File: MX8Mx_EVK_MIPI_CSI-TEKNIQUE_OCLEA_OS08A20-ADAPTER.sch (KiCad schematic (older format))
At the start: 16 parts, among them J1 1888863-4, J2 3-1734592-2, U1 NLSX5014DTR2G, U2 SN74LVC1G14DRL

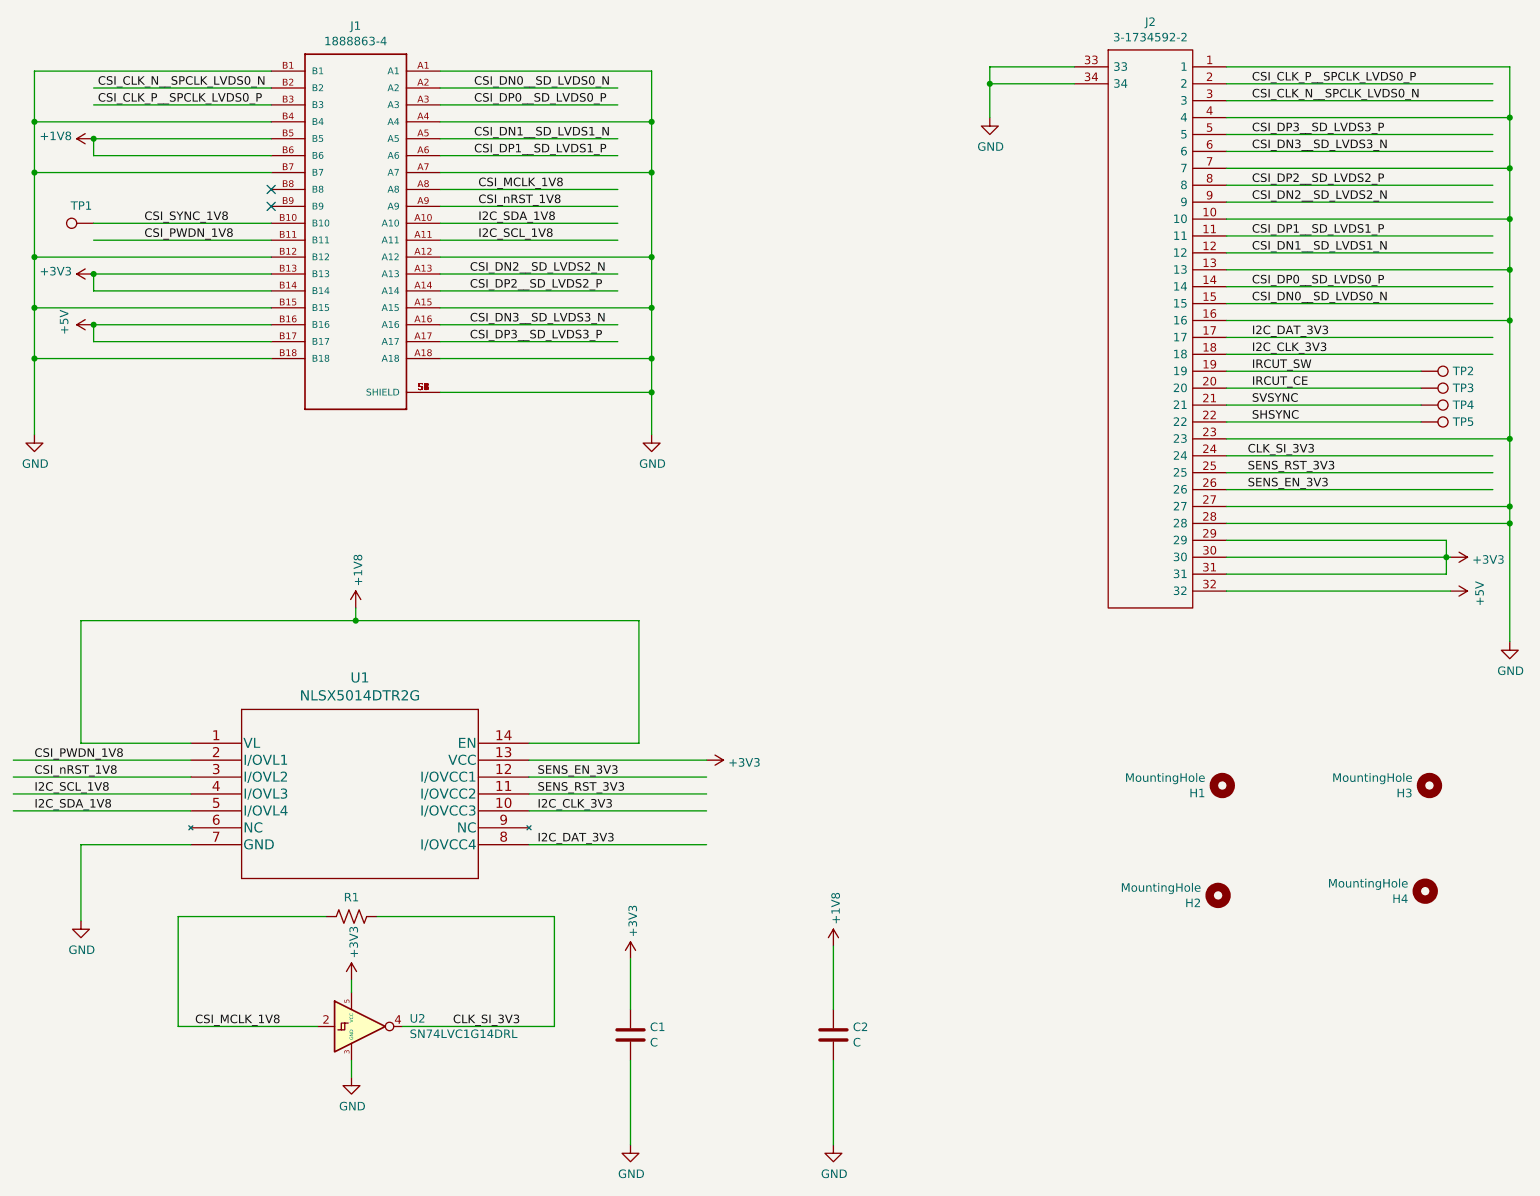
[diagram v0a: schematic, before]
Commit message: Update design with separate I2C and GPIO level translators
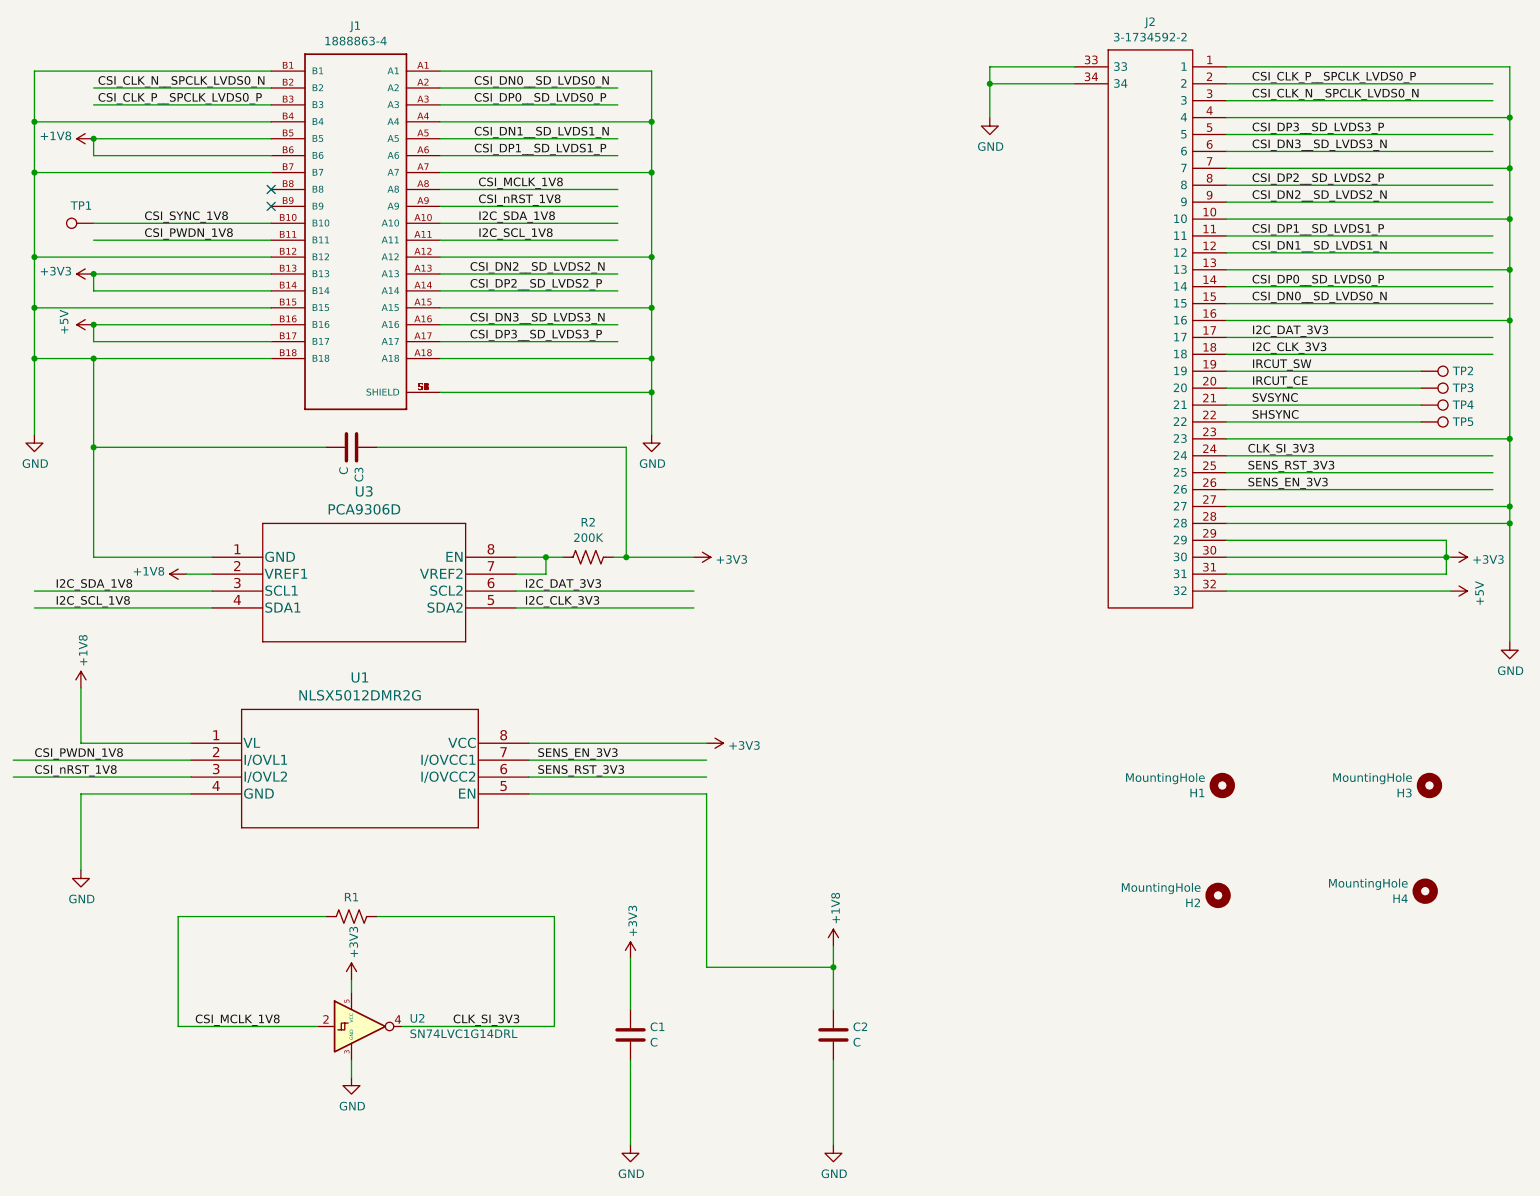
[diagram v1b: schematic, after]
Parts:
- removed U1: NLSX5014DTR2G, footprints:NLSX5014DTR2G, symbol NLSX5014DTR2G:NLSX5014DTR2G
- added C3: C, Capacitor_SMD:C_0603_1608Metric_Pad1.08x0.95mm_HandSolder, symbol Device:C
- added R2: 200K, Resistor_SMD:R_0805_2012Metric_Pad1.20x1.40mm_HandSolder, symbol Device:R_US
- added U1: NLSX5012DMR2G, footprints:NLSX5012DMR2G, symbol NLSX5012DMR2G:NLSX5012DMR2G
- added U3: PCA9306D, footprints:PCA9306D, symbol PCA9306D:PCA9306D_118
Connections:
- wire segments 129 -> 142
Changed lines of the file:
@@
 Sheet 1 1
 Title "Adapter for TEKNIQUE Oclea OS08a20 to MX8M Mini/Plus EVK"
-Date "2021-11-10"
-Rev "V1A"
+Date "2021-11-11"
+Rev "V1B"
 Comp "TuxVision"
 Comment1 ""
@@
 I2C_SCL_1V8
 $Comp
-L NLSX5014DTR2G:NLSX5014DTR2G U1
-U 1 1 6158CD6A
-P 1775 5050
-F 0 "U1" H 2775 5437 60  0000 C CNN
-F 1 "NLSX5014DTR2G" H 2775 5331 60  0000 C CNN
-F 2 "footprints:NLSX5014DTR2G" H 2775 5290 60  0001 C CNN
-F 3 "" H 1775 5050 60  0000 C CNN
-	1    1775 5050
-	1    0    0    -1
-$EndComp
-Wire Wire Line
-	4425 4325 4425 5050
-Wire Wire Line
-	4425 5050 3775 5050
-$Comp
 L power:+3V3 #PWR0112
 U 1 1 615AC6B3
-P 4825 5150
-F 0 "#PWR0112" H 4825 5000 50  0001 C CNN
-F 1 "+3V3" V 4840 5278 50  0000 L CNN
-F 2 "" H 4825 5150 50  0001 C CNN
-F 3 "" H 4825 5150 50  0001 C CNN
-	1    4825 5150
+P 4825 5050
+F 0 "#PWR0112" H 4825 4900 50  0001 C CNN
+F 1 "+3V3" V 4840 5178 50  0000 L CNN
+F 2 "" H 4825 5050 50  0001 C CNN
+F 3 "" H 4825 5050 50  0001 C CNN
+	1    4825 5050
 	0    1    1    0
 $EndComp
@@
 L power:+1V8 #PWR0113
 U 1 1 615E31C5
-P 2750 4250
-F 0 "#PWR0113" H 2750 4100 50  0001 C CNN
-F 1 "+1V8" V 2765 4378 50  0000 L CNN
-F 2 "" H 2750 4250 50  0001 C CNN
-F 3 "" H 2750 4250 50  0001 C CNN
-	1    2750 4250
-	1    0    0    -1
-$EndComp
-Wire Wire Line
-	2750 4250 2750 4325
-Connection ~ 2750 4325
-Wire Wire Line
-	2750 4325 4425 4325
-Wire Wire Line
-	1775 5450 725  5450
-Wire Wire Line
-	1775 5350 725  5350
-Wire Wire Line
-	1775 5150 725  5150
-Wire Wire Line
-	1775 5250 725  5250
-Wire Wire Line
-	4825 5650 3775 5650
-Wire Wire Line
-	4825 5450 3775 5450
+P 1125 4725
+F 0 "#PWR0113" H 1125 4575 50  0001 C CNN
+F 1 "+1V8" V 1140 4853 50  0000 L CNN
+F 2 "" H 1125 4725 50  0001 C CNN
+F 3 "" H 1125 4725 50  0001 C CNN
+	1    1125 4725
+	1    0    0    -1
+$EndComp
+Wire Wire Line
+	1900 4250 850  4250
+Wire Wire Line
+	1900 4150 850  4150
+Wire Wire Line
+	4750 4250 3700 4250
+Wire Wire Line
+	4750 4150 3700 4150
+Wire Wire Line
+	4825 5150 3775 5150
 Wire Wire Line
 	4825 5250 3775 5250
 Wire Wire Line
-	4825 5350 3775 5350
-Wire Wire Line
-	1775 5650 1125 5650
+	1775 5350 1125 5350
 $Comp
 L power:GND #PWR0114
 U 1 1 61678323
-P 1125 6100
-F 0 "#PWR0114" H 1125 5850 50  0001 C CNN
-F 1 "GND" H 1130 5927 50  0000 C CNN
-F 2 "" H 1125 6100 50  0001 C CNN
-F 3 "" H 1125 6100 50  0001 C CNN
-	1    1125 6100
-	1    0    0    -1
-$EndComp
-Wire Wire Line
-	1125 5650 1125 6100
-Wire Wire Line
-	1125 5050 1125 4325
-Wire Wire Line
-	1125 5050 1775 5050
-Wire Wire Line
-	1125 4325 2750 4325
-Text Label 850  5450 0    50   ~ 0
+P 1125 5800
+F 0 "#PWR0114" H 1125 5550 50  0001 C CNN
+F 1 "GND" H 1130 5627 50  0000 C CNN
+F 2 "" H 1125 5800 50  0001 C CNN
+F 3 "" H 1125 5800 50  0001 C CNN
+	1    1125 5800
+	1    0    0    -1
+$EndComp
+Wire Wire Line
+	1125 5350 1125 5800
+Text Label 975  4250 0    50   ~ 0
+I2C_SCL_1V8
+Text Label 975  4150 0    50   ~ 0
 I2C_SDA_1V8
-Text Label 850  5350 0    50   ~ 0
-I2C_SCL_1V8
-Text Label 3825 5450 0    50   ~ 0
+Text Label 3750 4150 0    50   ~ 0
+I2C_DAT_3V3
+Text Label 3750 4250 0    50   ~ 0
 I2C_CLK_3V3
-Text Label 3825 5650 0    50   ~ 0
-I2C_DAT_3V3
-Text Label 850  5150 0    50   ~ 0
-CSI_PWDN_1V8
-Text Label 850  5250 0    50   ~ 0
-CSI_nRST_1V8
+Text Label 3825 5150 0    50   ~ 0
+SENS_EN_3V3
 Text Label 3825 5250 0    50   ~ 0
-SENS_EN_3V3
-Text Label 3825 5350 0    50   ~ 0
 SENS_RST_3V3
 $Comp
@@
 	1    0    0    -1
 $EndComp
-Wire Wire Line
-	5575 6250 5575 6625
 $Comp
 L 1888863-4:1888863-4 J1
@@
 $EndComp
 Wire Wire Line
-	850  2775 2250 2775
+	850  2775 1200 2775
 Wire Wire Line
 	3250 2975 4500 2975
@@
 	4300 1275 3250 1275
 Wire Wire Line
-	3775 5150 4825 5150
+	3775 5050 4825 5050
 $Comp
 L Connector:TestPoint TP1
@@
 Wire Wire Line
 	6500 1150 7000 1150
+$Comp
+L NLSX5012DMR2G:NLSX5012DMR2G U1
+U 1 1 618CE481
+P 1775 5050
+F 0 "U1" H 2775 5437 60  0000 C CNN
+F 1 "NLSX5012DMR2G" H 2775 5331 60  0000 C CNN
+F 2 "footprints:NLSX5012DMR2G" H 2775 5290 60  0001 C CNN
+F 3 "" H 1775 5050 60  0000 C CNN
+	1    1775 5050
+	1    0    0    -1
+$EndComp
+Text Label 850  5250 0    50   ~ 0
+CSI_nRST_1V8
+Text Label 850  5150 0    50   ~ 0
+CSI_PWDN_1V8
+Wire Wire Line
+	1775 5250 725  5250
+Wire Wire Line
+	1775 5150 725  5150
+Wire Wire Line
+	5575 6250 5575 6375
+Wire Wire Line
+	4825 5350 4825 6375
+Wire Wire Line
+	4825 6375 5575 6375
+Connection ~ 5575 6375
+Wire Wire Line
+	5575 6375 5575 6625
+Wire Wire Line
+	3775 5350 4825 5350
+Wire Wire Line
+	1125 4725 1125 5050
+Wire Wire Line
+	1125 5050 1775 5050
+$Comp
+L PCA9306D:PCA9306D_118 U3
+U 1 1 6193C4E0
+P 1900 3950
+F 0 "U3" H 2800 4337 60  0000 C CNN
+F 1 "PCA9306D" H 2800 4231 60  0000 C CNN
+F 2 "footprints:PCA9306D" H 2800 4190 60  0001 C CNN
+F 3 "" H 1900 3950 60  0000 C CNN
+	1    1900 3950
+	1    0    0    -1
+$EndComp
+Wire Wire Line
+	1200 2775 1200 3300
+Wire Wire Line
+	1200 3950 1900 3950
+Connection ~ 1200 2775
+Wire Wire Line
+	1200 2775 2250 2775
+$Comp
+L power:+3V3 #PWR0102
+U 1 1 6198300F
+P 4750 3950
+F 0 "#PWR0102" H 4750 3800 50  0001 C CNN
+F 1 "+3V3" V 4765 4078 50  0000 L CNN
+F 2 "" H 4750 3950 50  0001 C CNN
+F 3 "" H 4750 3950 50  0001 C CNN
+	1    4750 3950
+	0    1    1    0
+$EndComp
+$Comp
+L power:+1V8 #PWR0103
+U 1 1 6198CDAF
+P 1750 4050
+F 0 "#PWR0103" H 1750 3900 50  0001 C CNN
+F 1 "+1V8" V 1765 4178 50  0000 L CNN
+F 2 "" H 1750 4050 50  0001 C CNN
+F 3 "" H 1750 4050 50  0001 C CNN
+	1    1750 4050
+	0    -1   -1   0
+$EndComp
+Wire Wire Line
+	1900 4050 1750 4050
+$Comp
+L Device:C C3
+U 1 1 619AC978
+P 2725 3300
+F 0 "C3" H 2840 3346 50  0000 L CNN
+F 1 "C" H 2840 3255 50  0000 L CNN
+F 2 "Capacitor_SMD:C_0603_1608Metric_Pad1.08x0.95mm_HandSolder" H 2763 3150 50  0001 C CNN
+F 3 "~" H 2725 3300 50  0001 C CNN
+	1    2725 3300
+	0    1    1    0
+$EndComp
+Wire Wire Line
+	2575 3300 1200 3300
+Connection ~ 1200 3300
+Wire Wire Line
+	1200 3300 1200 3950
+$Comp
+L Device:R_US R2
+U 1 1 619C89CA
+P 4125 3950
+F 0 "R2" V 3920 3950 50  0000 C CNN
+F 1 "200K" V 4011 3950 50  0000 C CNN
+F 2 "Resistor_SMD:R_0805_2012Metric_Pad1.20x1.40mm_HandSolder" V 4165 3940 50  0001 C CNN
+F 3 "~" H 4125 3950 50  0001 C CNN
+	1    4125 3950
+	0    1    1    0
+$EndComp
+Wire Wire Line
+	4275 3950 4350 3950
+Wire Wire Line
+	2875 3300 4350 3300
+Wire Wire Line
+	4350 3300 4350 3950
+Connection ~ 4350 3950
+Wire Wire Line
+	4350 3950 4750 3950
+Wire Wire Line
+	3700 3950 3875 3950
+Wire Wire Line
+	3700 4050 3875 4050
+Wire Wire Line
+	3875 4050 3875 3950
+Connection ~ 3875 3950
+Wire Wire Line
+	3875 3950 3975 3950
 $EndSCHEMATC
